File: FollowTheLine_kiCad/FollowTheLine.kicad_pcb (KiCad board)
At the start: 2 copper layers, 12 parts, among them J1 Conn_01x02_Pin, J2 Conn_01x06_Pin, J3 Conn_01x03_Pin, J4 Conn_01x05_Pin, J5 Conn_01x02_Pin, U1 ARDUINO_PRO_MINI, U3 L7805

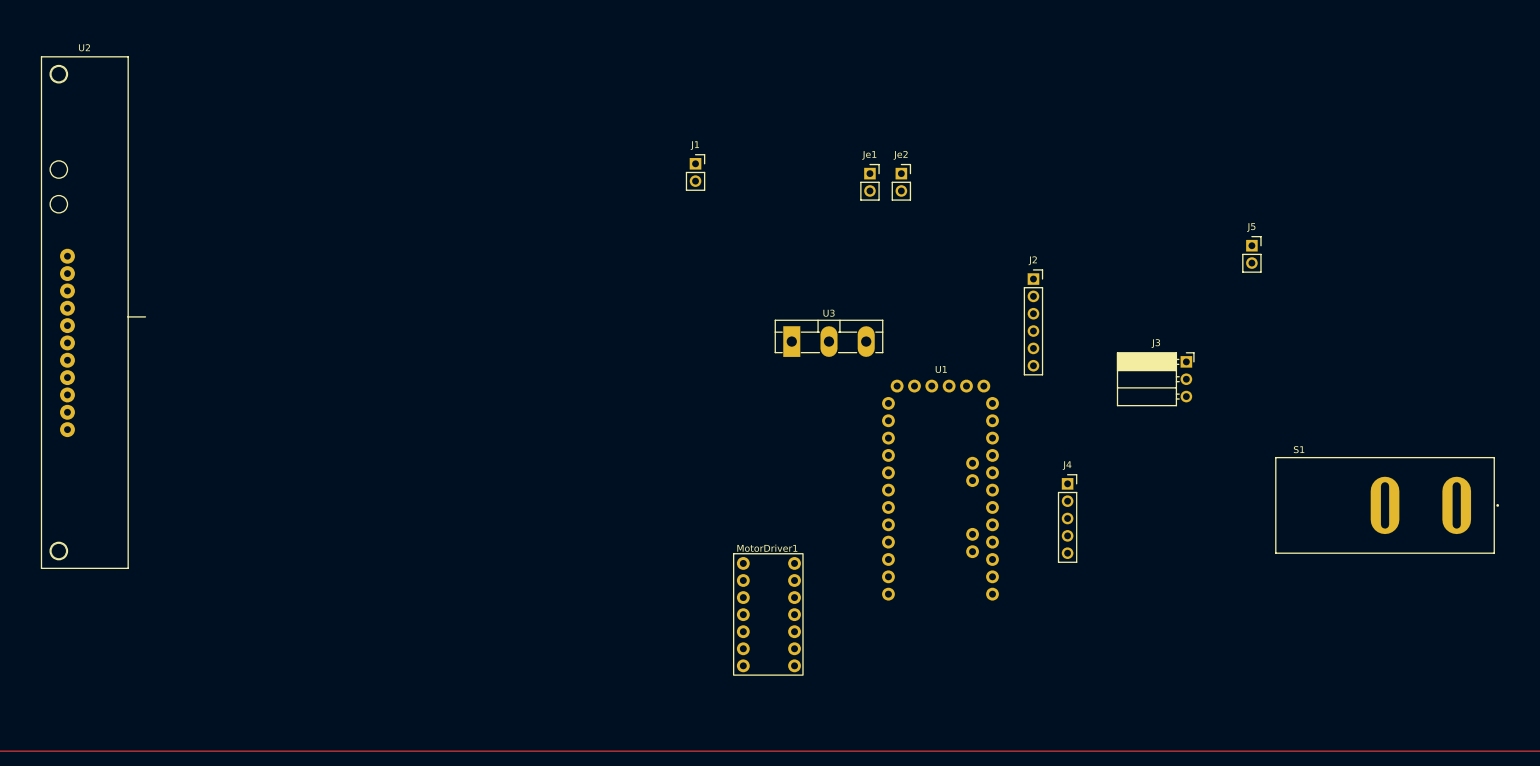
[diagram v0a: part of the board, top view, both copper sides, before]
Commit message: First version of follow the line pcb - only schematic
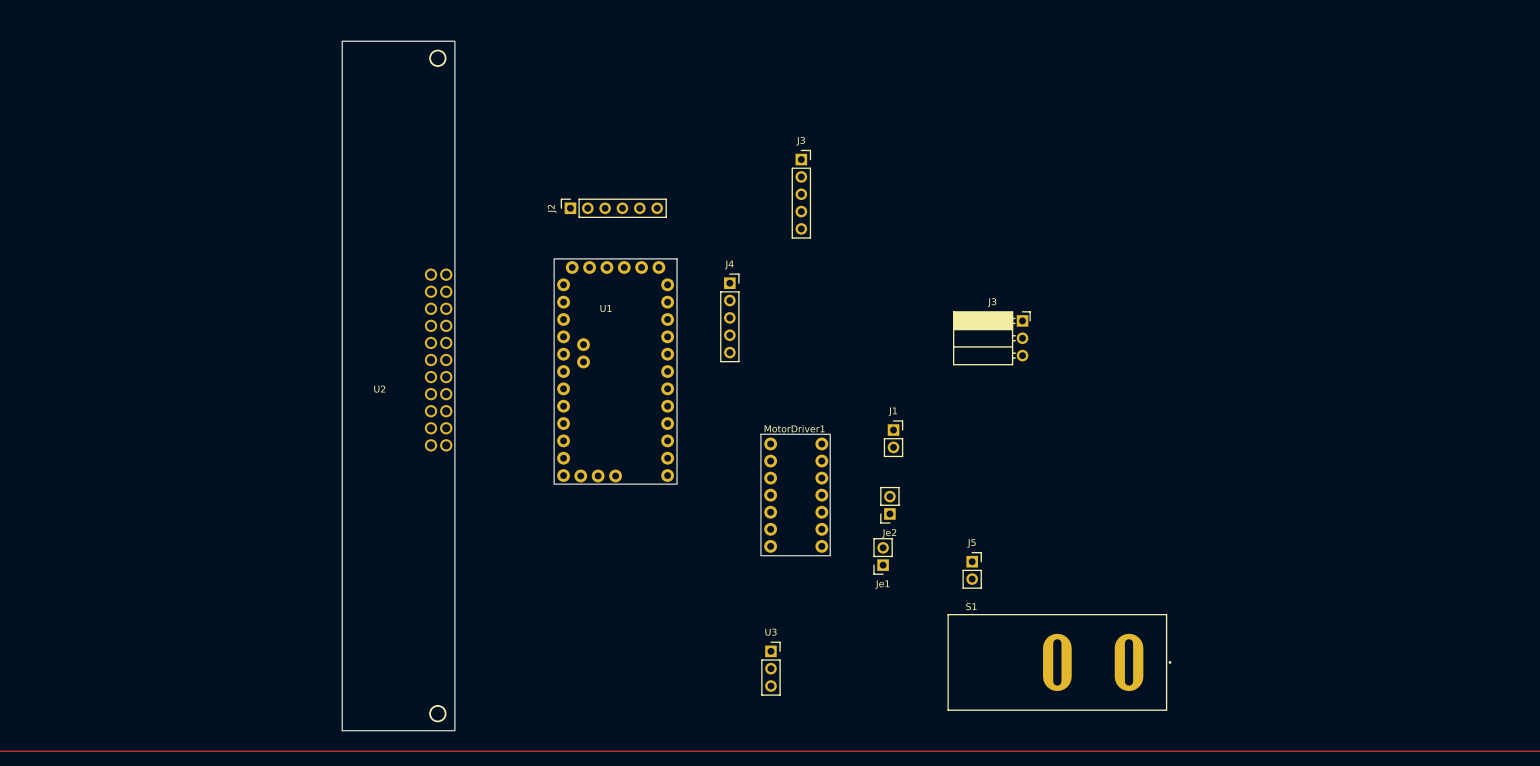
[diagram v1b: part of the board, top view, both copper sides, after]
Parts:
- added J3: Conn_01x05, Connector_PinSocket_2.54mm:PinSocket_1x05_P2.54mm_Vertical, F.Cu at (148.0, 53.3)
- U3: footprint Package_TO_SOT_THT:TO-3P-3_Vertical -> Connector_PinSocket_2.54mm:PinSocket_1x03_P2.54mm_Vertical
- moved U2 90.2 mm to (86.0, 137.0)
- moved J2 68.6 mm to (114.2, 60.5), turned to 90 degrees
- moved J5 61.8 mm to (173.0, 112.2)
- moved J4 57.5 mm to (137.5, 71.5)
- moved Je1 57.4 mm to (160.0, 112.8), turned to 180 degrees
- moved S1 53.2 mm to (185.5, 127.0)
- moved Je2 49.9 mm to (161.0, 105.2), turned to 180 degrees
- moved J1 48.6 mm to (161.5, 93.0)
- moved U3 45.5 mm to (143.6, 125.4)
- moved U1 38.4 mm to (130.0, 100.9)
- moved J3 24.7 mm to (180.4, 77.0)
- moved MotorDriver1 10.5 mm to (142.1, 111.4)
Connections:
- MotorDriver1 pad AENBL: Net-(U1-D5) -> Net-(MotorDriver1-PadAENBL)
- MotorDriver1 pad APHASE: Net-(U1-D3) -> Net-(MotorDriver1-PadAPHASE)
- MotorDriver1 pad Aout1: (no net) -> Net-(Je2-Pin_1)
- MotorDriver1 pad Aout2: (no net) -> Net-(Je2-Pin_2)
- MotorDriver1 pad BENBL: Net-(U1-D9) -> Net-(MotorDriver1-PadBENBL)
- MotorDriver1 pad BPHASE: Net-(U1-D6) -> Net-(MotorDriver1-PadBPHASE)
- MotorDriver1 pad Bout1: (no net) -> Net-(J1-Pin_1)
- MotorDriver1 pad Bout2: (no net) -> Net-(J1-Pin_2)
- MotorDriver1 pad VCC: +5V -> VCC
- MotorDriver1 pad VCC_HightVolt: (no net) -> GND2
- MotorDriver1 pad VMM: (no net) -> Net-(Je1-Pin_2)
- S1 pad 1: +12V -> Net-(J5-POS)
- S1 pad 2: Net-(U3-IN) -> +12V
- U2 pad LED1: (no net) -> Net-(U1-PadA0)
- U2 pad LED2: Net-(U1-A1) -> Net-(U1-PadA1)
- U2 pad LED3: Net-(U1-A2) -> Net-(U1-PadA2)
- U2 pad LED4: Net-(U1-A3) -> Net-(U1-PadA3)
- U2 pad LED5: Net-(U1-A4) -> Net-(U1-PadA4)
- U2 pad LED6: Net-(U1-A5) -> Net-(U1-PadA5)
- U2 pad LED7: Net-(U1-A6) -> Net-(U1-PadA6)
- U2 pad LED8: Net-(U1-A7) -> Net-(U1-PadA7)
- U3 pad 1: Net-(U3-IN) -> +12V
- U3 pad 2: GND1 -> GND2
- U3 pad 3: +5V -> VCC
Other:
- board outline added: 16.5 x 101 mm

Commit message: Follow the line. PCB version v2
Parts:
- removed the J3 at (148.0, 53.3)
- removed the J3 at (180.4, 77.0)
- removed Je1, Je2: Conn_01x02_Pin, Connector_PinSocket_2.54mm:PinSocket_1x02_P2.54mm_Vertical
- removed MotorDriver1: DRV8835, Library:DRV8835
- removed U1: ARDUINO_PRO_MINI, ARDUINO_PRO_MINI:MODULE_ARDUINO_PRO_MINI
- added ?: , , F.Cu at (337.0, 195.0)
- added ?: , , F.Cu at (355.0, 195.0)
- added ?: , , F.Cu at (355.0, 78.0)
- added ?: , , F.Cu at (337.0, 78.0)
- added A1: Arduino_Nano_Every, Module:Arduino_Nano, F.Cu at (319.7, 118.1)
- added J18: Socket_02, Connector_PinSocket_2.54mm:PinSocket_1x02_P2.54mm_Vertical, F.Cu at (356.3, 165.7)
- added J3: Socket_02, Connector_PinSocket_2.54mm:PinSocket_1x02_P2.54mm_Vertical, F.Cu at (342.5, 165.7)
- added J6: Socket_02, Connector_PinSocket_2.54mm:PinSocket_1x02_P2.54mm_Vertical, F.Cu at (351.7, 165.7)
- added J7: Socket_06, Connector_PinSocket_2.54mm:PinSocket_1x06_P2.54mm_Vertical, F.Cu at (333.3, 172.8)
- J1, J5: value Conn_01x02_Pin -> Socket_02
- J2: value Conn_01x06_Pin -> Socket_02; footprint Connector_PinSocket_2.54mm:PinSocket_1x06_P2.54mm_Vertical -> Connector_PinSocket_2.54mm:PinSocket_1x02_P2.54mm_Vertical
- J4: value Conn_01x05_Pin -> Screw_Terminal; footprint Connector_PinSocket_2.54mm:PinSocket_1x05_P2.54mm_Vertical -> TerminalBlock_Phoenix:TerminalBlock_Phoenix_PTSM-0,5-2-2.5-V-THR_1x02_P2.50mm_Vertical
- U2: value ~ -> Array Reflectance Sensor; footprint QTR-8A:QTR-8A -> QTRX-13RC:QTRX-13RC
- moved J2 247.2 mm to (337.9, 165.7), turned to 0 degrees
- moved J4 230.9 mm to (343.6, 175.6)
- moved U3 200.1 mm to (337.9, 172.8)
- moved J1 186.5 mm to (333.3, 165.7)
- moved J5 182.1 mm to (347.1, 165.7)
- moved S1 145.4 mm to (330.1, 142.0)
- moved U2 86.1 mm to (172.1, 136.0)
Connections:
- J4 pad 2: Net-(J4-Pin_2) -> GND2
- J5 pad 1: +12V -> /pin1_qtrx_in (TX)
- J5 pad 2: GND1 -> /pin13_qtrx_in (RX)
- S1 pad 1: Net-(J5-POS) -> Net-(J4-Pin_1)
- U2 pad EVEN: Net-(U1-PadD8) -> /pin13_EVEN
- U2 pad LED1: Net-(U1-PadA0) -> /QTRX_pin1_out
- U2 pad LED10: Net-(U1-PadD12) -> /led10
- U2 pad LED11: Net-(U1-PadD11) -> /Led11
- U2 pad LED12: Net-(U1-PadD10) -> /Led12
- U2 pad LED13: Net-(U1-PadD4) -> /QTRX_pin13_out
- U2 pad LED2: Net-(U1-PadA1) -> /led2
- U2 pad LED3: Net-(U1-PadA2) -> /Led3
- U2 pad LED4: Net-(U1-PadA3) -> /Led4
- U2 pad LED5: Net-(U1-PadA4) -> /Led5
- U2 pad LED6: Net-(U1-PadA5) -> /pin11_led6
- U2 pad LED7: Net-(U1-PadA6) -> /pin12_led7
- U2 pad LED8: Net-(U1-PadA7) -> /Led8
- U2 pad LED9: Net-(U1-PadD13) -> /Led9
- U2 pad ODD: Net-(U1-PadD7) -> /ODD
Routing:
- net (no net): vias 0 -> 1
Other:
- board size 16.5 x 101 mm -> 211.6 x 141.7 mm

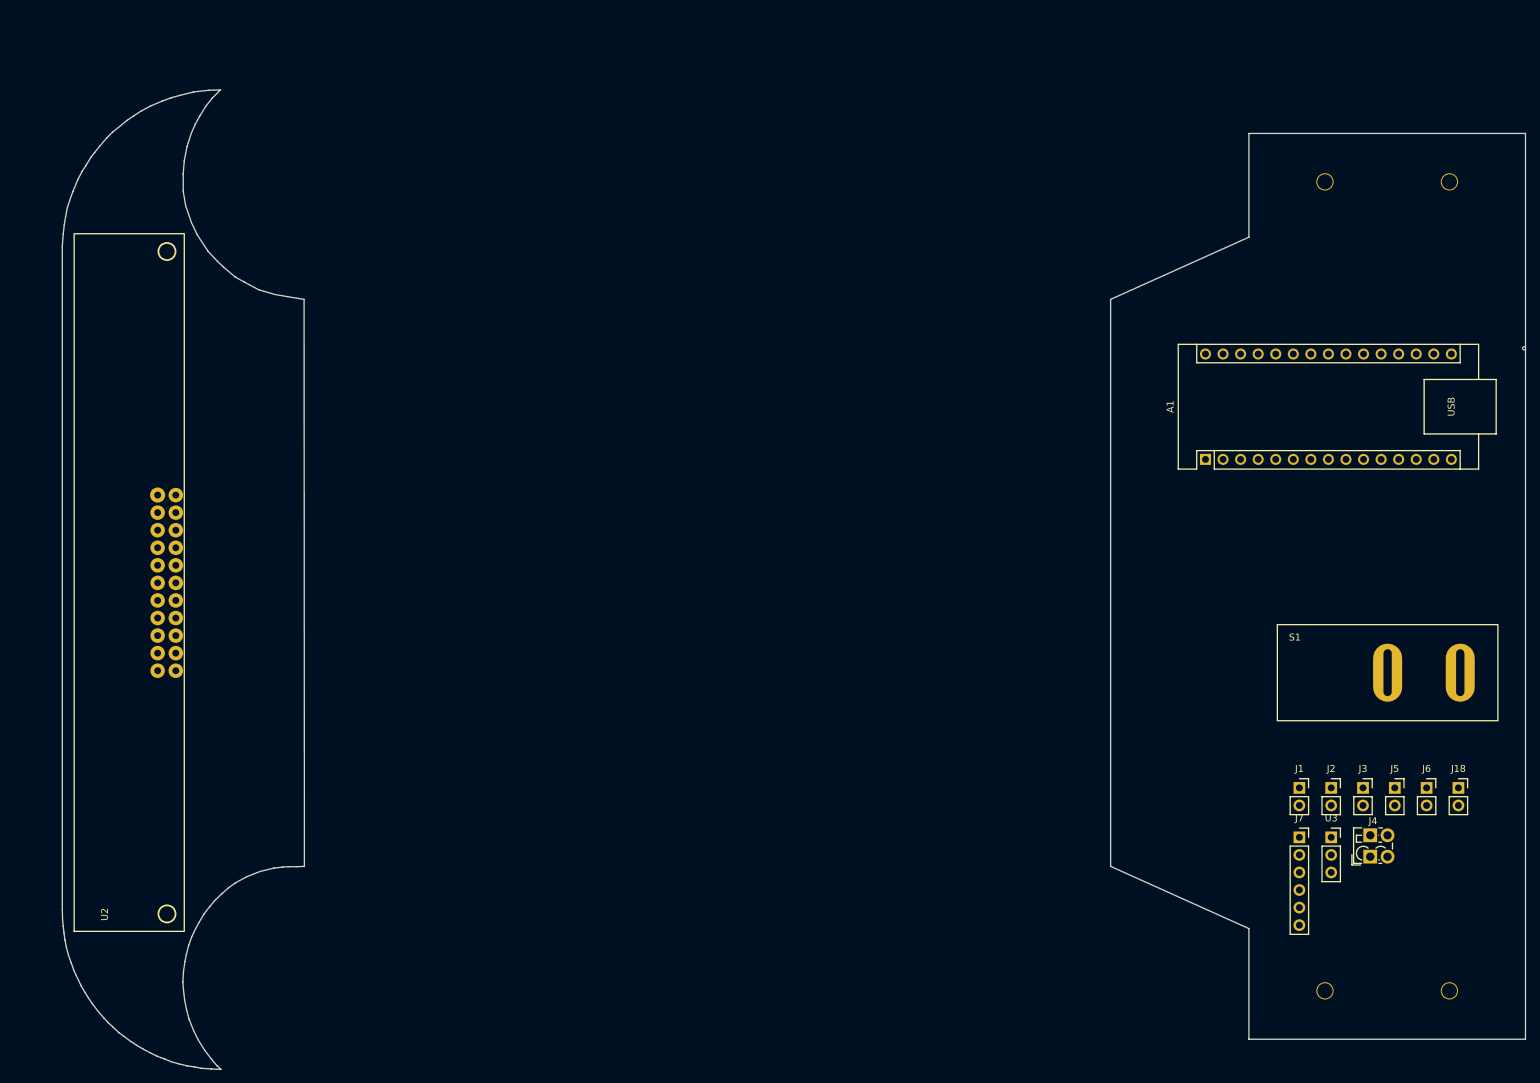
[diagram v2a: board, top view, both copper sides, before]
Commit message: kicad footprint version 2
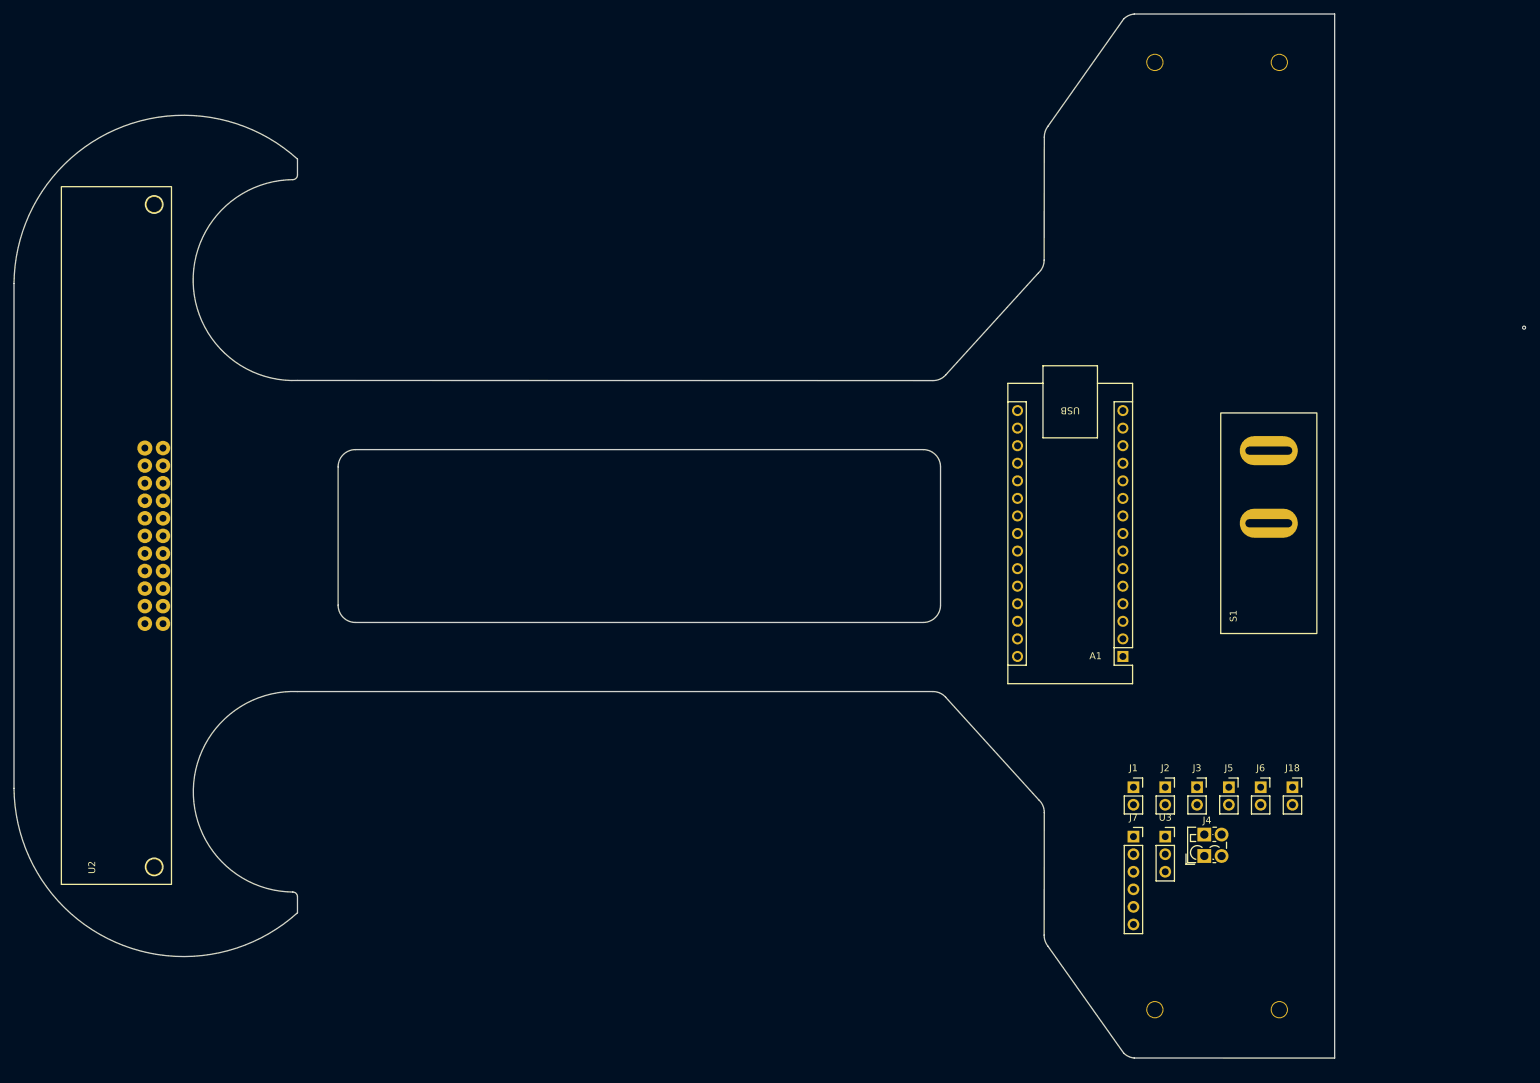
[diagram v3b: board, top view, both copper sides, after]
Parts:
- removed the ? at (337.0, 195.0)
- removed the ? at (355.0, 195.0)
- removed the ? at (355.0, 78.0)
- removed the ? at (337.0, 78.0)
- added ?: , , F.Cu at (330.4, 197.7)
- added ?: , , F.Cu at (330.4, 60.7)
- added ?: , , F.Cu at (312.4, 197.7)
- added ?: , , F.Cu at (312.4, 60.7)
- moved A1 30.9 mm to (307.8, 146.6), turned to 180 degrees
- moved J1 24.0 mm to (309.3, 165.6)
- moved J18 24.0 mm to (332.3, 165.6)
- moved J2 24.0 mm to (313.9, 165.6)
- moved J3 24.0 mm to (318.5, 165.6)
- moved J4 24.0 mm to (319.6, 175.5)
- moved J5 24.0 mm to (323.1, 165.6)
- moved J6 24.0 mm to (327.7, 165.6)
- moved J7 24.0 mm to (309.3, 172.7)
- moved U3 24.0 mm to (313.9, 172.7)
- moved S1 8.30 mm to (321.9, 143.3), turned to 90 degrees
- moved U2 7.05 mm to (170.2, 129.2)
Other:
- board size 211.6 x 141.7 mm -> 191 x 151 mm

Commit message: pcb completed
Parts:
- removed J7: Socket_06, Connector_PinSocket_2.54mm:PinSocket_1x06_P2.54mm_Vertical
- added ?: , , F.Cu at (84.0, 96.6)
- added ?: , , F.Cu at (84.0, 81.9)
- added A6: SW_Push, Button_Switch_THT:SW_PUSH_6mm, F.Cu at (229.1, 83.2)
- added A7: SW_Push, Button_Switch_THT:SW_PUSH_6mm, F.Cu at (228.8, 98.8)
- added J9: Socket_04, Connector_PinSocket_2.54mm:PinSocket_1x04_P2.54mm_Vertical, F.Cu at (228.2, 109.5)
- added MotorDriver1: DRV8835, Library:DRV8835, F.Cu at (214.2, 60.9)
- added R1: 1kΩ, Resistor_THT:R_Axial_DIN0204_L3.6mm_D1.6mm_P5.08mm_Horizontal, F.Cu at (234.2, 95.6)
- added R2: 1kΩ, Resistor_THT:R_Axial_DIN0204_L3.6mm_D1.6mm_P5.08mm_Horizontal, F.Cu at (230.3, 95.5)
- J4: footprint TerminalBlock_Phoenix:TerminalBlock_Phoenix_PTSM-0,5-2-2.5-V-THR_1x02_P2.50mm_Vertical -> TerminalBlock_Phoenix:TerminalBlock_Phoenix_MPT-0,5-2-2.54_1x02_P2.54mm_Horizontal
- moved J4 169.2 mm to (208.3, 48.0), turned to -90 degrees
- moved J1 149.4 mm to (236.2, 35.2)
- moved J3 141.5 mm to (230.6, 54.7), turned to 90 degrees
- moved U3 140.3 mm to (216.9, 71.3), turned to -90 degrees
- moved J18 131.0 mm to (204.7, 135.7), turned to -90 degrees
- moved J5 123.5 mm to (204.7, 130.5), turned to -90 degrees
- moved A1 120.7 mm to (206.4, 81.1), turned to 0 degrees
- moved J6 110.9 mm to (228.2, 116.4), turned to 180 degrees
- moved S1 108.2 mm to (237.7, 75.5)
- moved ? 105.9 mm to (232.4, 157.7)
- moved ? 105.9 mm to (232.4, 20.7)
- moved ? 105.9 mm to (214.4, 157.7)
- moved ? 105.9 mm to (214.4, 20.7)
- moved U2 105.9 mm to (72.2, 89.2)
- moved J2 81.5 mm to (236.0, 141.5), turned to 180 degrees
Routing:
- net GND: track 0.00 -> 258.3 mm, vias 0 -> 4
- net VCC: track 0.00 -> 210.3 mm
- net /pin13_EVEN: track 0.00 -> 196.4 mm, vias 0 -> 2
- net /QTRX_pin1_out: track 0.00 -> 180.5 mm, vias 0 -> 2
- net /led10: track 0.00 -> 175.3 mm, vias 0 -> 7
- net /Led8: track 0.00 -> 175.2 mm, vias 0 -> 1
- net /Led12: track 0.00 -> 170.9 mm, vias 0 -> 3
- net /pin11_led6: track 0.00 -> 165.9 mm, vias 0 -> 2
- net /led2: track 0.00 -> 165.2 mm, vias 0 -> 1
- net /Led4: track 0.00 -> 160.9 mm, vias 0 -> 3
- net /Led9: track 0.00 -> 157.0 mm, vias 0 -> 1
- net /Led11: track 0.00 -> 153.6 mm
- net /QTRX_pin13_out: track 0.00 -> 152.2 mm
- net /Led3: track 0.00 -> 147.1 mm
- net /pin12_led7: track 0.00 -> 146.5 mm
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- added copper zone on B.Cu, net GND
- added copper zone on F.Cu, net GND
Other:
- outline, holes or cut-outs redrawn
- board text added: "13/ 1"
- board text added: "3V/5V"
- board text added: "Bill Tsol"
- board text added: "RX/TX"
- board text added: "VM/MD"
- board text added: "Vcc/Gnd"
- board text added: "ref/A5/RST/RST"
